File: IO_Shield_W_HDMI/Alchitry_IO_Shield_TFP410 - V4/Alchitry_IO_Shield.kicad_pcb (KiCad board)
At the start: 4 copper layers, 65 x 45 mm, 66 parts, among them J0 HDMI_A_1.4, Q1 Q_PMOS_SGD, Q2 Q_PMOS_SGD, Q3 Q_PMOS_SGD, SW1 SW_DIP_x08, SW2 SW_DIP_x08, U0 boardmezzanine_new, U1 TFP410

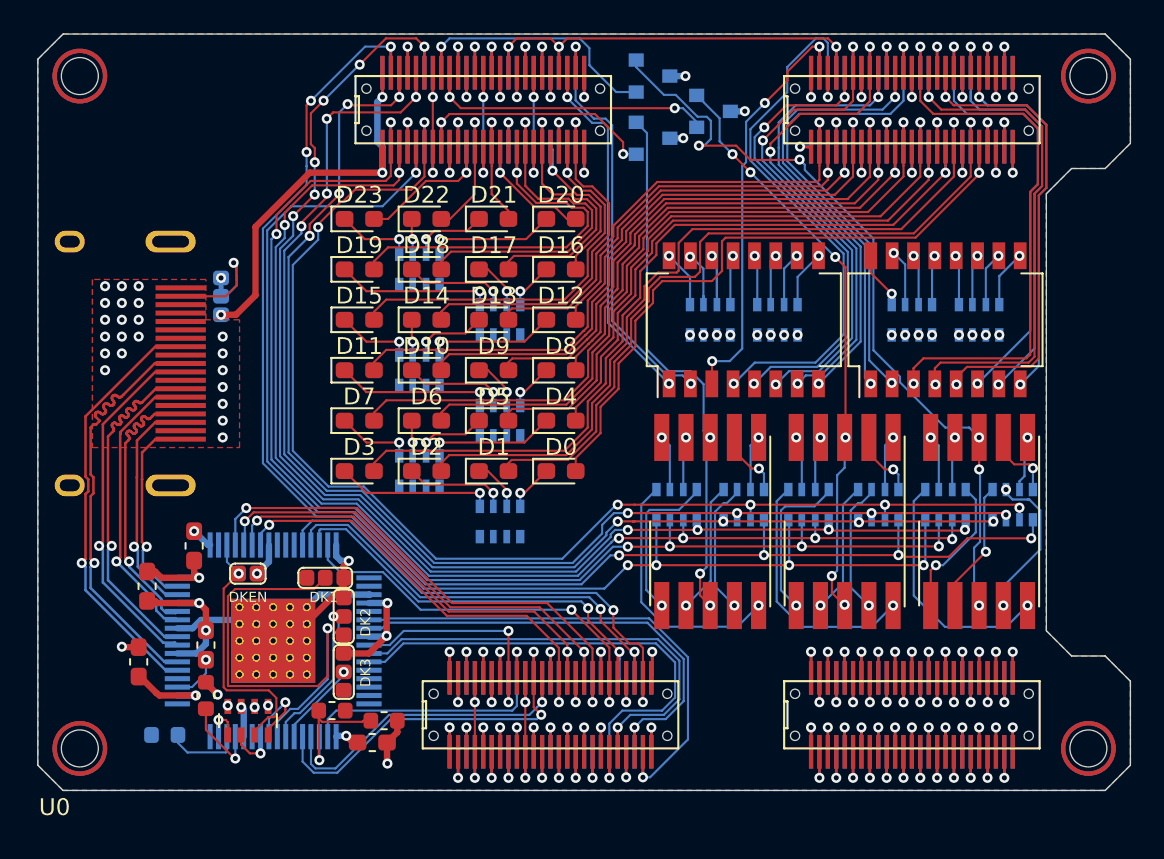
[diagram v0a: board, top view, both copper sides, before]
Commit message: removed islands
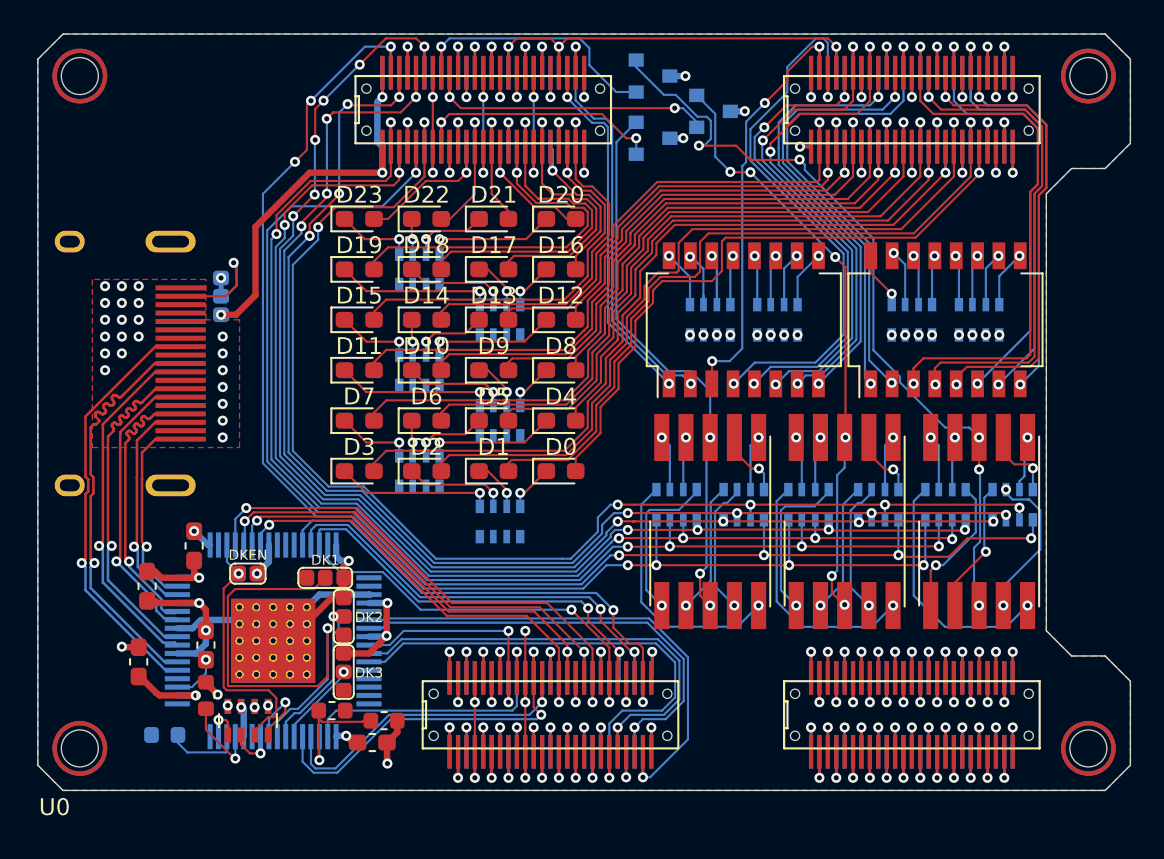
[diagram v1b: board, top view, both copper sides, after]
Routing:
- net GNDREF: track 163.4 -> 166.2 mm, vias 62 -> 63
- net Net-(AFF3-Pad3): track 31.8 -> 32.8 mm
- net /C1: track 76.2 -> 76.9 mm
- net Net-(AFF2-Pad3): track 34.7 -> 35.4 mm
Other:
- board text added: "AYEEDITYA"
